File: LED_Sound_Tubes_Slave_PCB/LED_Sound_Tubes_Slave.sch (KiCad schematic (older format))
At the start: 50 parts, among them IC1 4050D, J2 Teensy_3_2_Header, P1 POWER + DATA, P10 LED_STR_4, P11 LED_STR_5, P2 +5V, P3 0V, P4 +5V, P5 0V, P6 LED_STR_1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

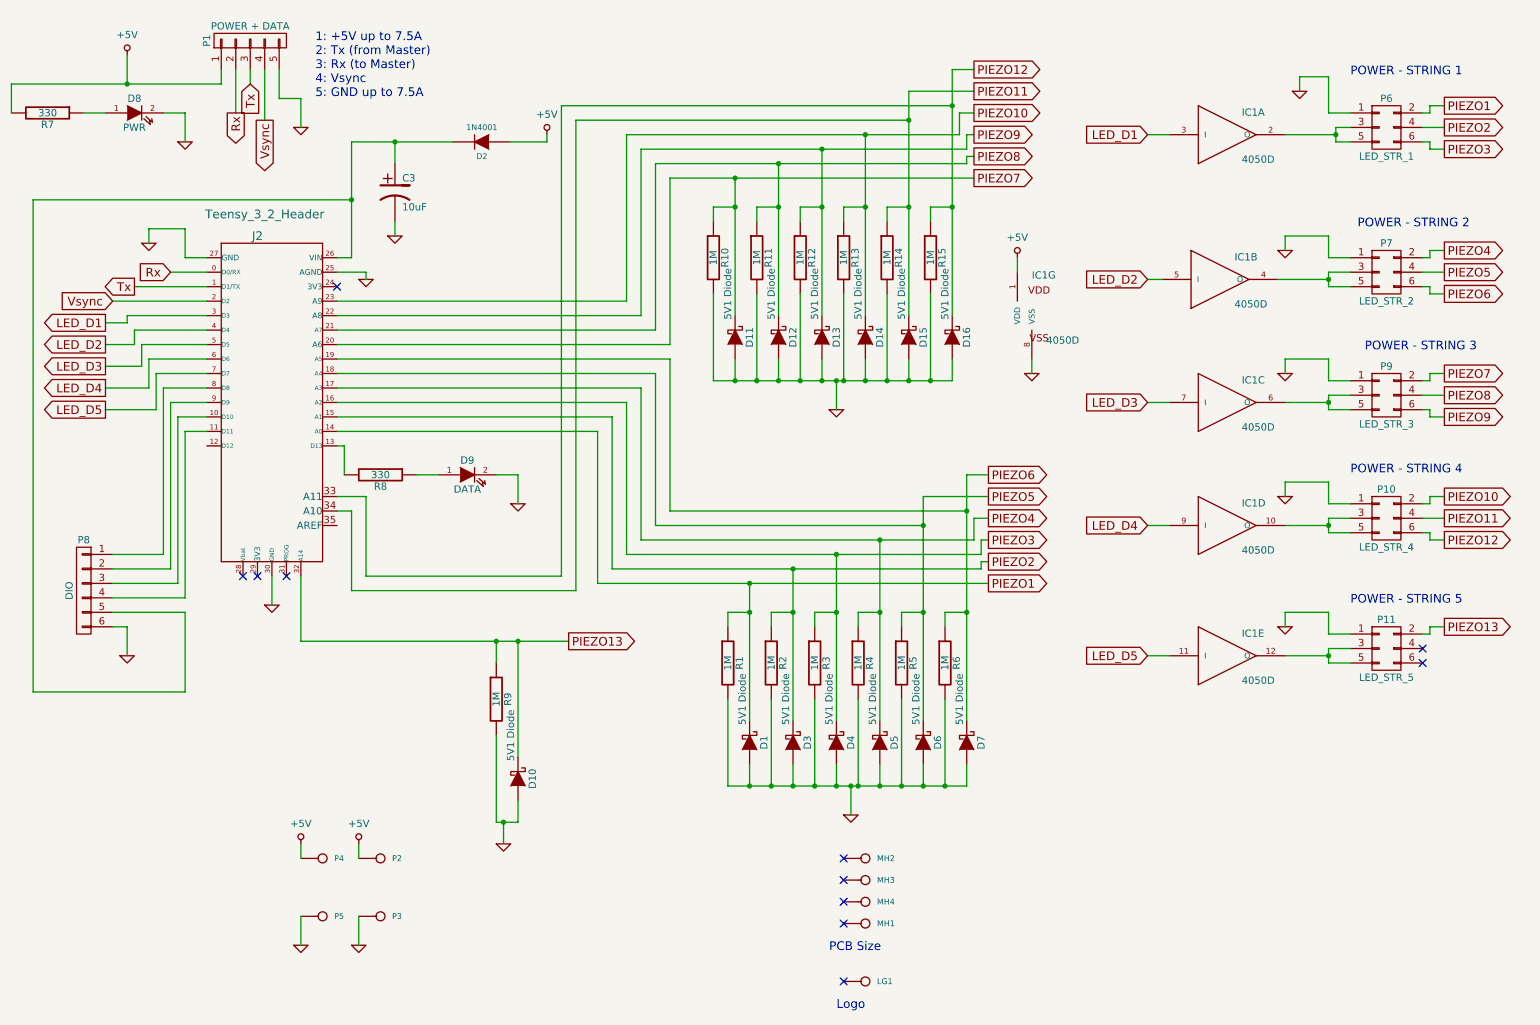
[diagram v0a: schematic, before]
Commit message: New PCB with filters
Added filters. Total redesign of PCB
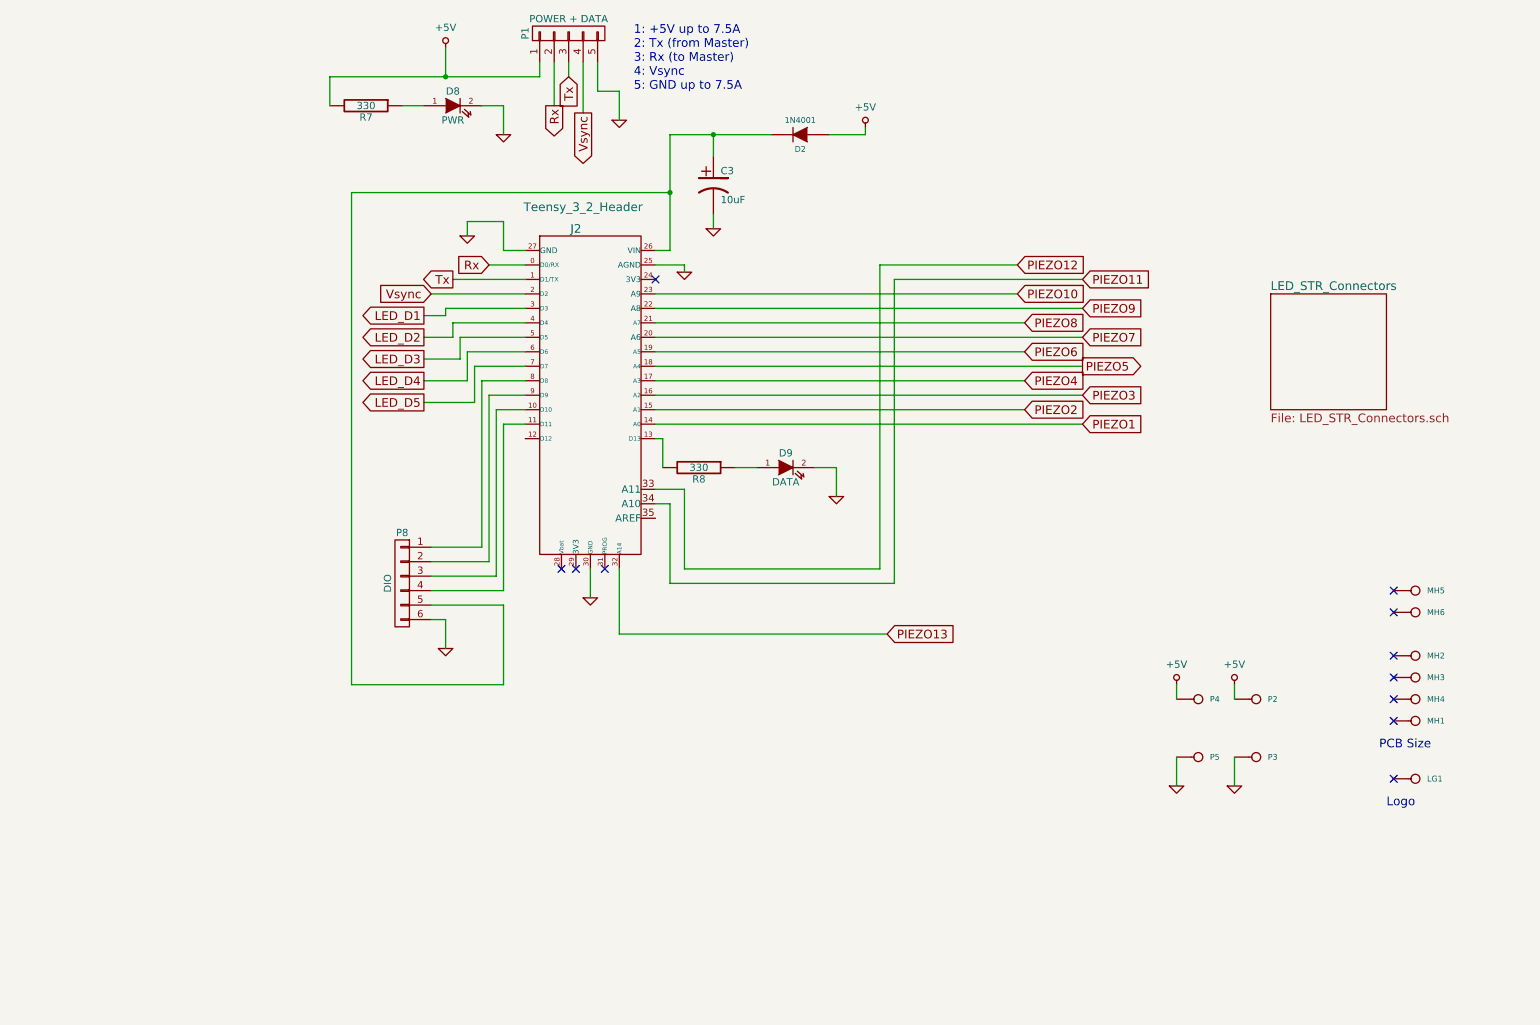
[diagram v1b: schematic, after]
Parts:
- removed D1, D10, D11, D12, D13, D14, D15, D16, D3, D4, D5, D6, D7: 5V1 Diode, REInnovationFootprint:TH_Diode_3, symbol D_Schottky
- removed IC1: 4050D, REInnovationFootprint:DIP-16__NARROW, symbol 4050D
- removed P10: LED_STR_4, REInnovationFootprint:IDC_Header_6W_2.54, symbol CONN_02X03
- removed P11: LED_STR_5, REInnovationFootprint:IDC_Header_6W_2.54, symbol CONN_02X03
- removed P6: LED_STR_1, REInnovationFootprint:IDC_Header_6W_2.54, symbol CONN_02X03
- removed P7: LED_STR_2, REInnovationFootprint:IDC_Header_6W_2.54, symbol CONN_02X03
- removed P9: LED_STR_3, REInnovationFootprint:IDC_Header_6W_2.54, symbol CONN_02X03
- removed R1, R10, R11, R12, R13, R14, R15, R2, R3, R4, R5, R6, R9: 1M, REInnovationFootprint:TH_Resistor_1, symbol R
- added MH5, MH6: CONN_1, REInnovationFootprint:3mm_hole, symbol CONN_1
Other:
- note removed: "POWER - STRING 1"
- note removed: "POWER - STRING 2"
- note removed: "POWER - STRING 3"
- note removed: "POWER - STRING 4"
- note removed: "POWER - STRING 5"
- moved on the sheet: C3, D2, D8, D9, J2, LG1, MH1, MH2, MH3, MH4, P1, P2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
